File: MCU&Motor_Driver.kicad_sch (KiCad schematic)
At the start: 19 parts, among them J1 Conn_01x07_Pin, J2 Conn_01x02_Socket, J3 Conn_01x04_Pin, J4 Conn_01x03_Pin, U1 ADAFRUIT_QT_PY, U3 TMC2208-LA

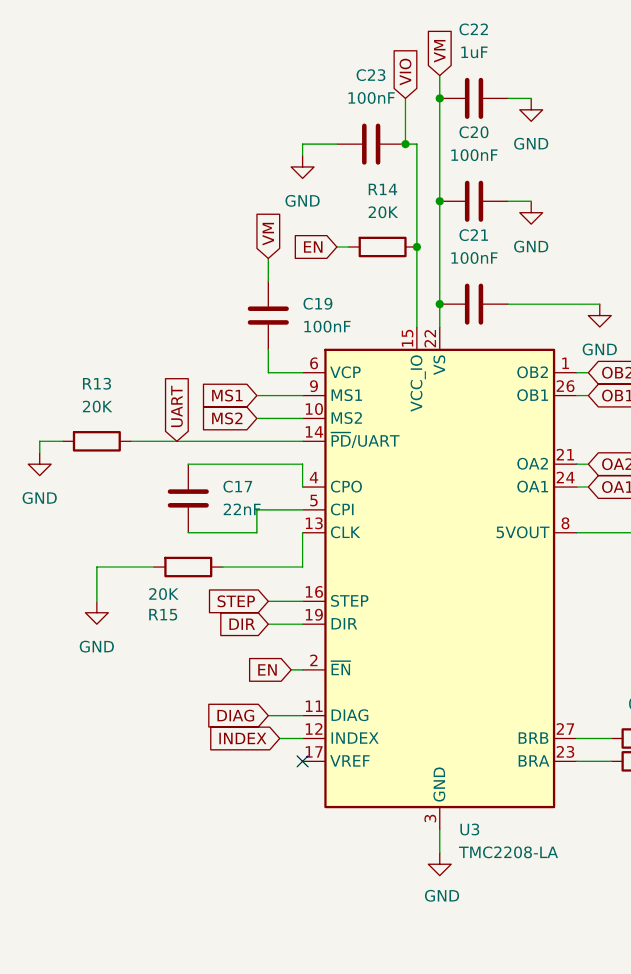
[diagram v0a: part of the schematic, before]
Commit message: Added a voltage divider to the vref pin on the TMC2208 such as to limit the max current to 0.5A based of the NEMA 14 motor I am using this for and also grounded the EN pin on the TMC2208 as to not have the need to add a GPIO connection to the ESP32 to have also that controlled since that would put too much constraints on the design and would be troublesome.
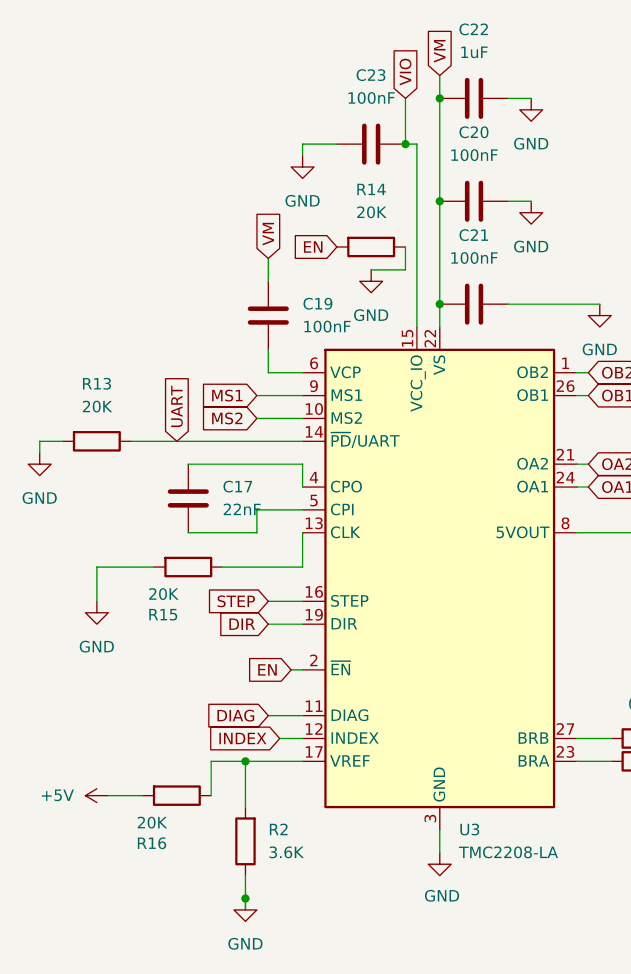
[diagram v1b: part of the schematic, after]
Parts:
- added R16: 20K, Resistor_SMD:R_0402_1005Metric, symbol Device:R
- added R2: 3.6K, Resistor_SMD:R_0402_1005Metric, symbol Device:R
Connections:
- net +5V: now also R16.2
- net GND: now also R14.1, R2.1
- net VIO: no longer R14.1
- net at U3.17 (VREF): now also R16.1, R2.2
- no-connect marks 1 -> 0
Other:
- moved on the sheet: R14
